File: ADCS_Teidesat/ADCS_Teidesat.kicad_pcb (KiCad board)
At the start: 4 copper layers, 90.2 x 95.9 mm, 27 parts, among them U1 MAX2659ELT+T, U2 L86-M33, U3 LSM6DSV16XTR, U4 LIS2MDLTR, U5 TMS5703137DPGEQQ1, Y1 ATX-H13-F-16.000MHz-G100-T

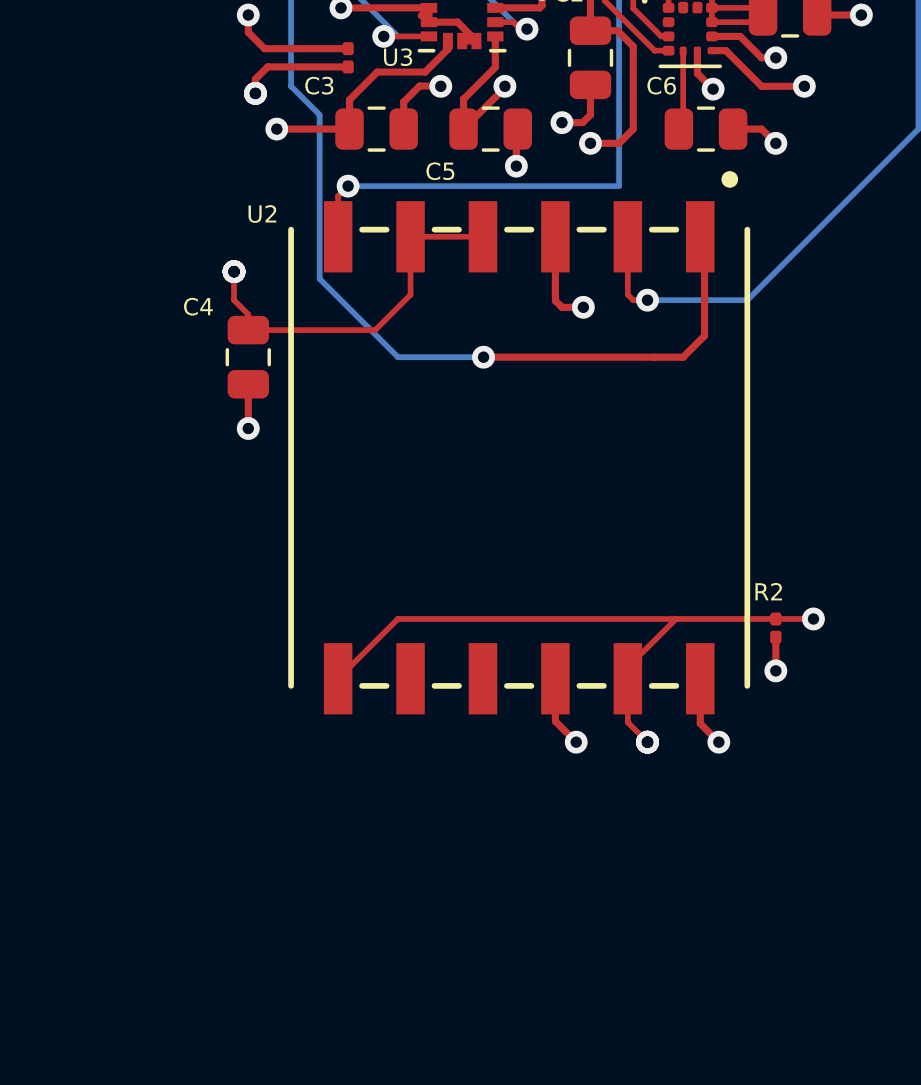
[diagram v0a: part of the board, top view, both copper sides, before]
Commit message: Modificación en la huella del módulo GNSS
He añadido un pin que añadimos en el esquemático al símbolo del modulo GNSS, el pin 13. Hemos añadido dicho pin a la huella del componente.

Co-Authored-By: hugohdezmo <238262256+hugohdezmo@users.noreply.github.com>
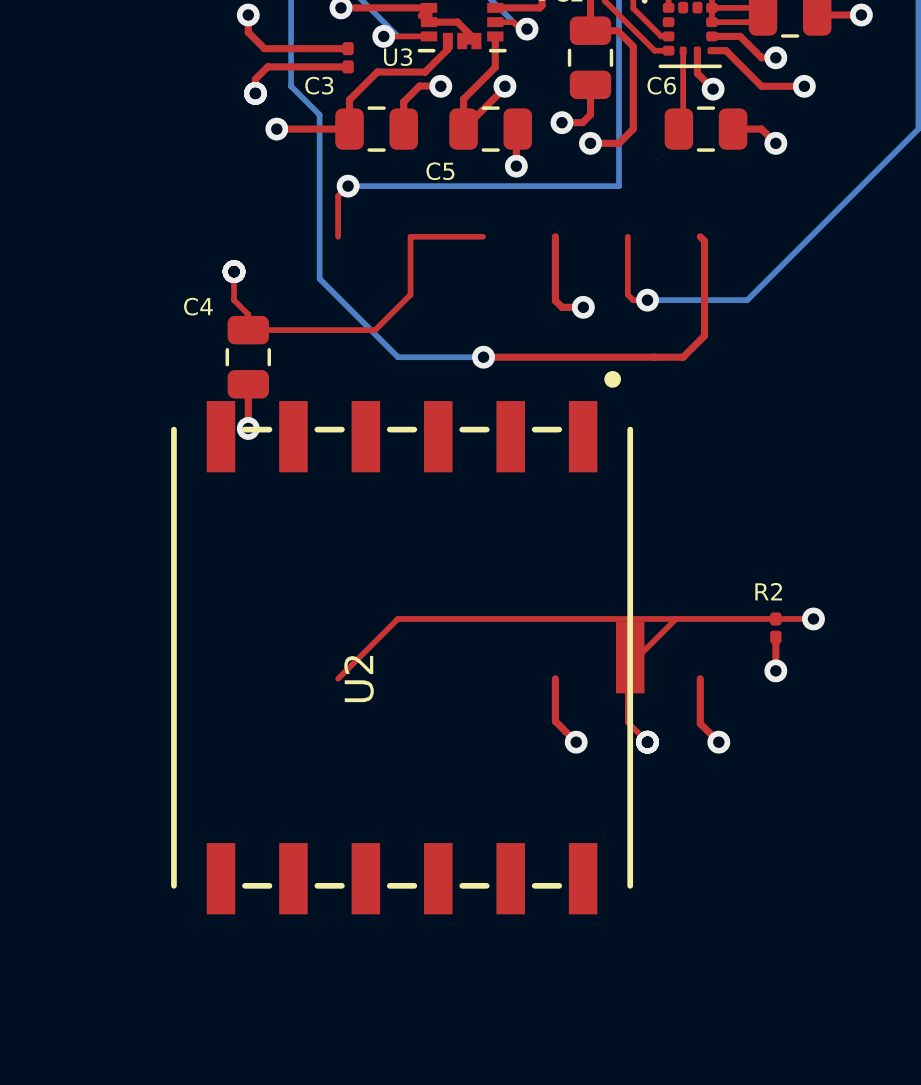
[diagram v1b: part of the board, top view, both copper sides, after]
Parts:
- U2: footprint Huellas ADCS:L80-M39 -> Huellas ADCS:Prueba_MODULOGNSS
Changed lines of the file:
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@@
 		)
 	)
-	(footprint "Huellas ADCS:L80-M39"
+	(footprint "Huellas ADCS:Prueba_MODULOGNSS"
 		(layer "F.Cu")
 		(at 141.92 125.27665 90)
-		(descr "L80-M39")
-		(tags "Integrated Circuit")
 		(property "Reference" "U2"
-			(at 16.27665 -3.92 180)
-			(layer "F.SilkS")
-			(effects
-				(font
-					(size 0.6 0.6)
-					(thickness 0.15)
+			(at 0 -0.5 90)
+			(unlocked yes)
+			(layer "F.SilkS")
+			(effects
+				(font
+					(size 1 1)
+					(thickness 0.1)
 				)
 			)
 		)
 		(property "Value" "L86-M33"
-			(at 7.154 4.997 90)
-			(layer "F.SilkS")
-			(hide yes)
-			(effects
-				(font
-					(size 1.27 1.27)
-					(thickness 0.254)
+			(at 0 1 90)
+			(unlocked yes)
+			(layer "F.Fab")
+			(hide yes)
+			(effects
+				(font
+					(size 1 1)
+					(thickness 0.15)
 				)
 			)
@@
 		(property "Datasheet" "https://datasheet.datasheetarchive.com/originals/distributors/Datasheets_SAMA/d9c8c7b89a7ac852e6b026dd2100f946.pdf"
 			(at 0 0 90)
-			(layer "F.Fab")
-			(hide yes)
-			(effects
-				(font
-					(size 1.27 1.27)
+			(unlocked yes)
+			(layer "F.Fab")
+			(hide yes)
+			(effects
+				(font
+					(size 1 1)
 					(thickness 0.15)
 				)
@@
 		(property "Description" "GPS/GLONASS receiver + antenna pack of 1"
 			(at 0 0 90)
-			(layer "F.Fab")
-			(hide yes)
-			(effects
-				(font
-					(size 1.27 1.27)
+			(unlocked yes)
+			(layer "F.Fab")
+			(hide yes)
+			(effects
+				(font
+					(size 1 1)
 					(thickness 0.15)
 				)
@@
 		(attr smd)
 		(fp_line
-			(start -0.25 -2.92)
-			(end 15.75 -2.92)
-			(stroke
-				(width 0.2)
-				(type solid)
-			)
-			(layer "F.SilkS")
-		)
-		(fp_line
-			(start 15.75 -0.43)
-			(end 15.75 0.43)
-			(stroke
-				(width 0.2)
-				(type solid)
-			)
-			(layer "F.SilkS")
-		)
-		(fp_line
-			(start -0.25 -0.43)
-			(end -0.25 0.43)
-			(stroke
-				(width 0.2)
-				(type solid)
-			)
-			(layer "F.SilkS")
-		)
-		(fp_line
-			(start 15.75 2.11)
-			(end 15.75 2.97)
-			(stroke
-				(width 0.2)
-				(type solid)
-			)
-			(layer "F.SilkS")
-		)
-		(fp_line
-			(start -0.25 2.11)
-			(end -0.25 2.97)
-			(stroke
-				(width 0.2)
-				(type solid)
-			)
-			(layer "F.SilkS")
-		)
-		(fp_line
-			(start 15.75 4.65)
-			(end 15.75 5.51)
-			(stroke
-				(width 0.2)
-				(type solid)
-			)
-			(layer "F.SilkS")
-		)
-		(fp_line
-			(start -0.25 4.65)
-			(end -0.25 5.51)
-			(stroke
-				(width 0.2)
-				(type solid)
-			)
-			(layer "F.SilkS")
-		)
-		(fp_line
-			(start 15.75 7.19)
-			(end 15.75 8.05)
-			(stroke
-				(width 0.2)
-				(type solid)
-			)
-			(layer "F.SilkS")
-		)
-		(fp_line
-			(start -0.25 7.19)
-			(end -0.25 8.05)
-			(stroke
-				(width 0.2)
-				(type solid)
-			)
-			(layer "F.SilkS")
-		)
-		(fp_line
-			(start 15.75 9.73)
-			(end 15.75 10.59)
-			(stroke
-				(width 0.2)
-				(type solid)
-			)
-			(layer "F.SilkS")
-		)
-		(fp_line
-			(start -0.25 9.73)
-			(end -0.25 10.59)
-			(stroke
-				(width 0.2)
-				(type solid)
-			)
-			(layer "F.SilkS")
-		)
-		(fp_line
-			(start -0.25 13.08)
-			(end 15.75 13.08)
+			(start -7.261 -7.0273)
+			(end 8.739 -7.0273)
+			(stroke
+				(width 0.2)
+				(type solid)
+			)
+			(layer "F.SilkS")
+		)
+		(fp_line
+			(start 8.739 -4.5373)
+			(end 8.739 -3.6773)
+			(stroke
+				(width 0.2)
+				(type solid)
+			)
+			(layer "F.SilkS")
+		)
+		(fp_line
+			(start -7.261 -4.5373)
+			(end -7.261 -3.6773)
+			(stroke
+				(width 0.2)
+				(type solid)
+			)
+			(layer "F.SilkS")
+		)
+		(fp_line
+			(start 8.739 -1.9973)
+			(end 8.739 -1.1373)
+			(stroke
+				(width 0.2)
+				(type solid)
+			)
+			(layer "F.SilkS")
+		)
+		(fp_line
+			(start -7.261 -1.9973)
+			(end -7.261 -1.1373)
+			(stroke
+				(width 0.2)
+				(type solid)
+			)
+			(layer "F.SilkS")
+		)
+		(fp_line
+			(start 8.739 0.5427)
+			(end 8.739 1.4027)
+			(stroke
+				(width 0.2)
+				(type solid)
+			)
+			(layer "F.SilkS")
+		)
+		(fp_line
+			(start -7.261 0.5427)
+			(end -7.261 1.4027)
+			(stroke
+				(width 0.2)
+				(type solid)
+			)
+			(layer "F.SilkS")
+		)
+		(fp_line
+			(start 8.739 3.0827)
+			(end 8.739 3.9427)
+			(stroke
+				(width 0.2)
+				(type solid)
+			)
+			(layer "F.SilkS")
+		)
+		(fp_line
+			(start -7.261 3.0827)
+			(end -7.261 3.9427)
+			(stroke
+				(width 0.2)
+				(type solid)
+			)
+			(layer "F.SilkS")
+		)
+		(fp_line
+			(start 8.739 5.6227)
+			(end 8.739 6.4827)
+			(stroke
+				(width 0.2)
+				(type solid)
+			)
+			(layer "F.SilkS")
+		)
+		(fp_line
+			(start -7.261 5.6227)
+			(end -7.261 6.4827)
+			(stroke
+				(width 0.2)
+				(type solid)
+			)
+			(layer "F.SilkS")
+		)
+		(fp_line
+			(start -7.261 8.9727)
+			(end 8.739 8.9727)
 			(stroke
 				(width 0.2)
@@
 		)
 		(fp_circle
-			(center 17.511 12.465)
-			(end 17.511 12.6073)
+			(center 10.5 8.3577)
+			(end 10.5 8.5)
 			(stroke
 				(width 0.3)
@@
 		)
 		(fp_line
-			(start 15.75 -2.92)
-			(end 15.75 13.08)
-			(stroke
-				(width 0.2)
-				(type solid)
-			)
-			(layer "F.Fab")
-		)
-		(fp_line
-			(start -0.25 -2.92)
-			(end 15.75 -2.92)
-			(stroke
-				(width 0.2)
-				(type solid)
-			)
-			(layer "F.Fab")
-		)
-		(fp_line
-			(start 15.75 13.08)
-			(end -0.25 13.08)
-			(stroke
-				(width 0.2)
-				(type solid)
-			)
-			(layer "F.Fab")
-		)
-		(fp_line
-			(start -0.25 13.08)
-			(end -0.25 -2.92)
+			(start 8.739 -7.0273)
+			(end 8.739 8.9727)
+			(stroke
+				(width 0.2)
+				(type solid)
+			)
+			(layer "F.Fab")
+		)
+		(fp_line
+			(start -7.261 -7.0273)
+			(end 8.739 -7.0273)
+			(stroke
+				(width 0.2)
+				(type solid)
+			)
+			(layer "F.Fab")
+		)
+		(fp_line
+			(start 8.739 8.9727)
+			(end -7.261 8.9727)
+			(stroke
+				(width 0.2)
+				(type solid)
+			)
+			(layer "F.Fab")
+		)
+		(fp_line
+			(start -7.261 8.9727)
+			(end -7.261 -7.0273)
 			(stroke
 				(width 0.2)
@@
 		)
 		(fp_text user "${REFERENCE}"
-			(at 7.154 4.997 90)
+			(at 0.143 0.8897 90)
 			(layer "F.Fab")
 			(effects
@@
 		)
 		(pad "1" smd rect
-			(at 15.5 11.43 180)
+			(at 8.489 7.3227 180)
 			(size 1 2.5)
 			(layers "F.Cu" "F.Mask" "F.Paste")
@@
 		)
 		(pad "2" smd rect
-			(at 15.5 8.89 180)
+			(at 8.489 4.7827 180)
 			(size 1 2.5)
 			(layers "F.Cu" "F.Mask" "F.Paste")
@@
 		)
 		(pad "3" smd rect
-			(at 15.5 6.35 180)
+			(at 8.489 2.2427 180)
 			(size 1 2.5)
 			(layers "F.Cu" "F.Mask" "F.Paste")
@@
 		)
 		(pad "4" smd rect
-			(at 15.5 3.81 180)
+			(at 8.489 -0.2973 180)
 			(size 1 2.5)
 			(layers "F.Cu" "F.Mask" "F.Paste")
@@
 		)
 		(pad "5" smd rect
-			(at 15.5 1.27 180)
+			(at 8.489 -2.8373 180)
 			(size 1 2.5)
 			(layers "F.Cu" "F.Mask" "F.Paste")
@@
 		)
 		(pad "6" smd rect
-			(at 15.5 -1.27 180)
+			(at 8.489 -5.3773 180)
 			(size 1 2.5)
 			(layers "F.Cu" "F.Mask" "F.Paste")
@@
 		)
 		(pad "7" smd rect
-			(at 0 -1.27 180)
+			(at -7.011 -5.3773 180)
 			(size 1 2.5)
 			(layers "F.Cu" "F.Mask" "F.Paste")
@@
 		)
 		(pad "8" smd rect
-			(at 0 1.27 180)
+			(at -7.011 -2.8373 180)
 			(size 1 2.5)
 			(layers "F.Cu" "F.Mask" "F.Paste")
@@
 		)
 		(pad "9" smd rect
-			(at 0 3.81 180)
+			(at -7.011 -0.2973 180)
 			(size 1 2.5)
 			(layers "F.Cu" "F.Mask" "F.Paste")
@@
 		)
 		(pad "10" smd rect
-			(at 0 6.35 180)
+			(at -7.011 2.2427 180)
 			(size 1 2.5)
 			(layers "F.Cu" "F.Mask" "F.Paste")
@@
 		)
 		(pad "11" smd rect
-			(at 0 8.89 180)
+			(at -7.011 4.7827 180)
 			(size 1 2.5)
 			(layers "F.Cu" "F.Mask" "F.Paste")
@@
 		)
 		(pad "12" smd rect
-			(at 0 11.43 180)
+			(at -7.011 7.3227 180)
 			(size 1 2.5)
 			(layers "F.Cu" "F.Mask" "F.Paste")
@@
 			(pintype "passive")
 		)
+		(pad "13" smd rect
+			(at 0.739 8.9727)
+			(size 1 2.5)
+			(layers "F.Cu" "F.Mask" "F.Paste")
+			(net 102 "/OUT_ANT")
+			(pinfunction "RF_IN")
+			(pintype "input")
+		)
 		(embedded_fonts no)
-		(model "C:/Users/aniba/OneDrive/Escritorio/TEIDESAT/ENTORNO DE TRABAJO/ultima versión/4CAPAS/componentes/L86-M33/L86-M33.stp"
-			(opacity 0.8700)
-			(offset
-				(xyz 7.8 -5.62 0)
-			)
-			(scale
-				(xyz 1 1 1)
-			)
-			(rotate
-				(xyz -90 -0 -0)
-			)
-		)
 	)
 	(footprint "Capacitor_SMD:C_0805_2012Metric"
